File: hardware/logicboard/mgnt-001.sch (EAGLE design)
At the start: 1 part

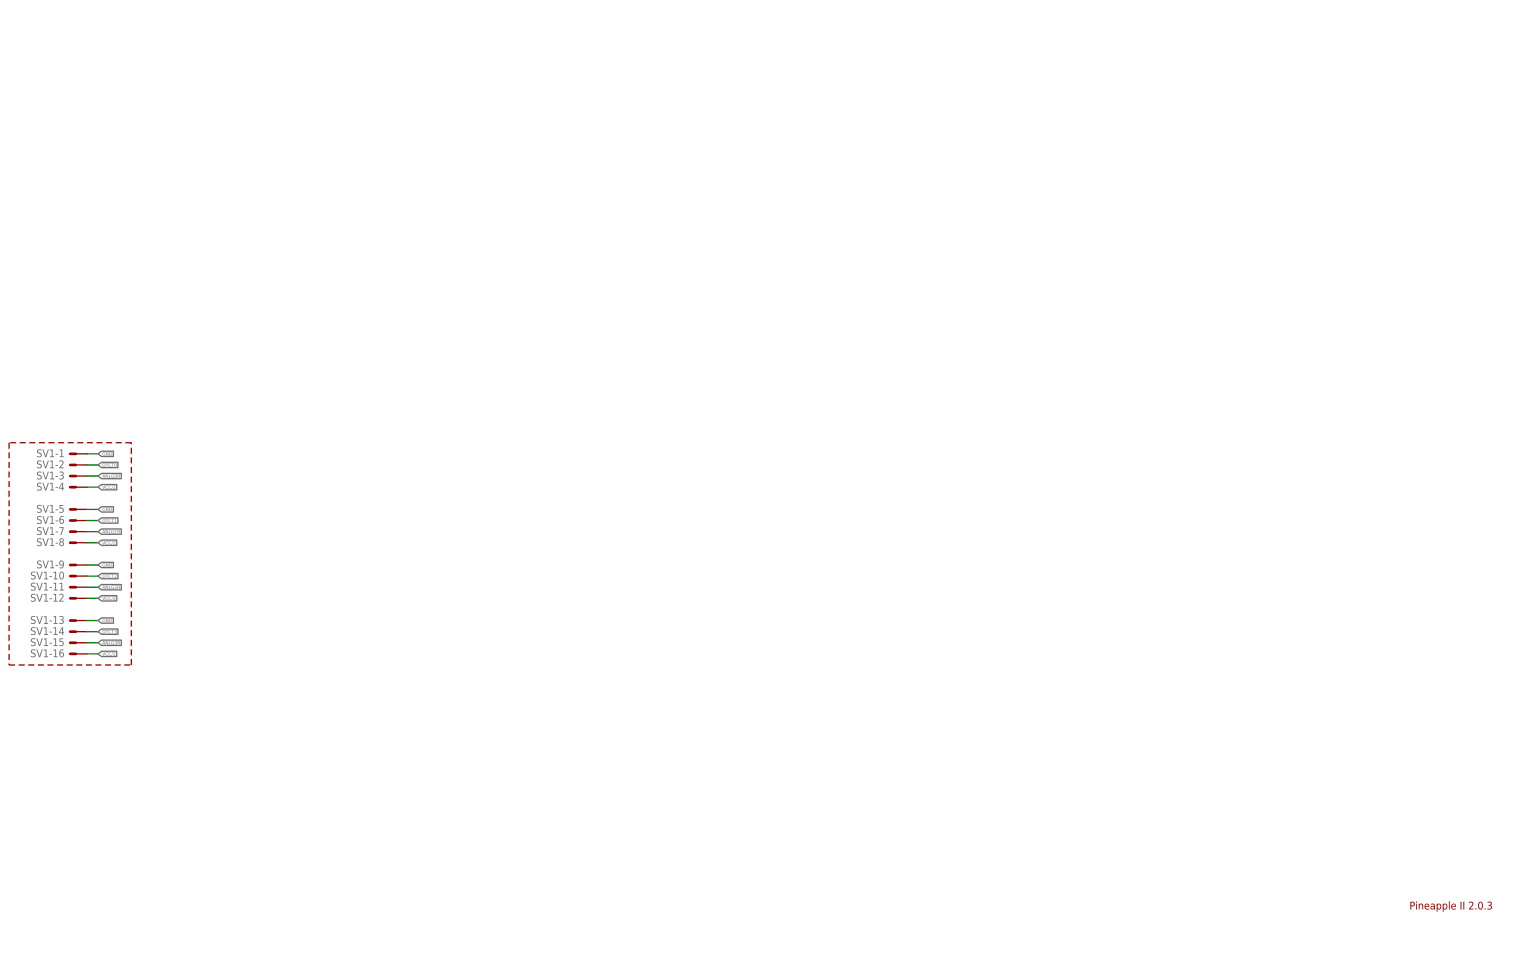
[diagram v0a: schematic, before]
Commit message: Placed reed sw and other parts.
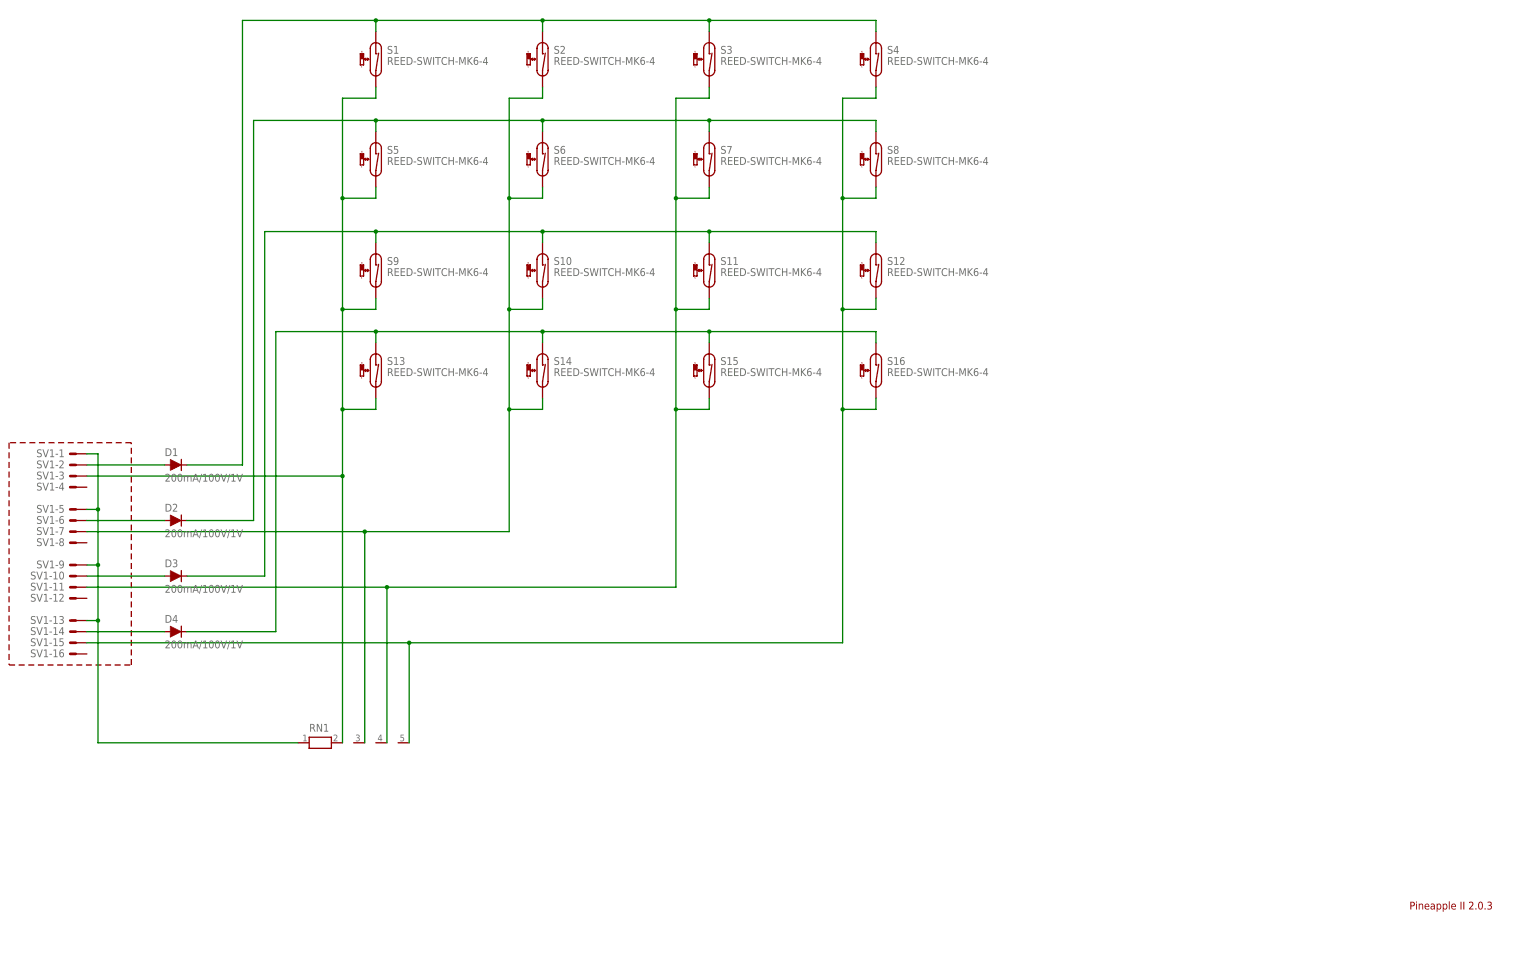
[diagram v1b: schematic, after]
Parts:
- added D1, D2, D3, D4: 200mA/100V/1V, SparkFun-DiscreteSemi:DIODE-1N4148
- added RN1: (no value), resistor-net:RN04
- added S1, S10, S11, S12, S13, S14, S15, S16, S2, S3, S4, S5, S6, S7, S8, S9: REED-SWITCH-MK6-4, switch-reed:REED-SWITCH-MK6-4
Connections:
- removed net ANLG0R: SV1-3.S
- removed net VCC/2: SV1-12.S, SV1-16.S, SV1-4.S, SV1-8.S
- new net N$1: D1.C, S1.1, S2.1, S3.1, S4.1
- new net N$2: D2.C, S5.1, S6.1, S7.1, S8.1
- new net N$3: D3.C, S10.1, S11.1, S12.1, S9.1
- new net N$4: D4.C, S13.1, S14.1, S15.1, S16.1
- new net N$5: RN1.2, S1.2, S13.2, S5.2, S9.2, SV1-3.S
- net ANLG1R: now also RN1.3, S10.2, S14.2, S2.2, S6.2
- net ANLG2R: now also RN1.4, S11.2, S15.2, S3.2, S7.2
- net ANLG3R: now also RN1.5, S12.2, S16.2, S4.2, S8.2
- net DTCT0: now also D1.A
- net DTCT1: now also D2.A
- net DTCT2: now also D3.A
- net DTCT3: now also D4.A
- net GND: now also RN1.1

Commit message: First try.
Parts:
- RN1: value (none) -> 103
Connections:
- net N$5 renamed ANLG0R
- removed net N$1: D1.C, S1.1, S2.1, S3.1, S4.1
- removed net N$2: D2.C, S5.1, S6.1, S7.1, S8.1
- removed net N$3: D3.C, S10.1, S11.1, S12.1, S9.1
- removed net N$4: D4.C, S13.1, S14.1, S15.1, S16.1
- net DTCT0: now also D1.C, S1.1, S2.1, S3.1, S4.1
- net DTCT1: now also D2.C, S5.1, S6.1, S7.1, S8.1
- net DTCT2: now also D3.C, S10.1, S11.1, S12.1, S9.1
- net DTCT3: now also D4.C, S13.1, S14.1, S15.1, S16.1

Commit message: Routed.
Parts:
- added U$1: PINEAPPLELOGO2, pineapplelogo:PINEAPPLELOGO2
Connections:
- new net DTCT0D: D1.C, S1.1, S2.1, S3.1, S4.1
- new net DTCT1D: D2.C, S5.1, S6.1, S7.1, S8.1
- new net DTCT2D: D3.C, S10.1, S11.1, S12.1, S9.1
- new net DTCT3D: D4.C, S13.1, S14.1, S15.1, S16.1
- net DTCT0: no longer D1.C, S1.1, S2.1, S3.1, S4.1
- net DTCT1: no longer D2.C, S5.1, S6.1, S7.1, S8.1
- net DTCT2: no longer D3.C, S10.1, S11.1, S12.1, S9.1
- net DTCT3: no longer D4.C, S13.1, S14.1, S15.1, S16.1
